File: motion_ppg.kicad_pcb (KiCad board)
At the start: 2 copper layers, 32.2 x 20.5 mm, 67 parts, among them P1 CONN_2, P2 CONN_2, P3 CONN_2, P4 CONN_1, P5 CONN_01X04, Q1 DMP21D5UFB4-7B, U1 TPS63001, U2 ADS1291/2, U3 NRF528XX-QFAA, U4 MPU-9250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

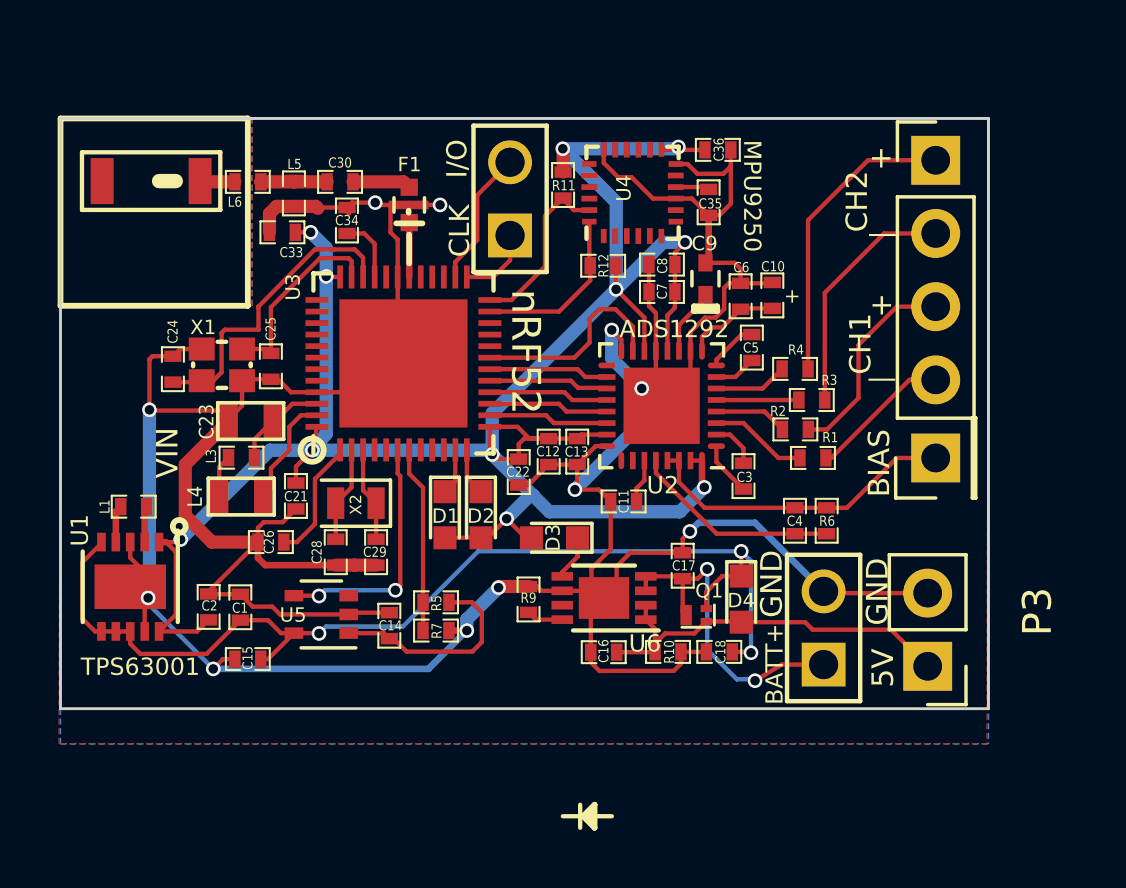
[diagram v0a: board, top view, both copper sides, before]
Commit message: Added new libs, removed load switch, added TPS62746
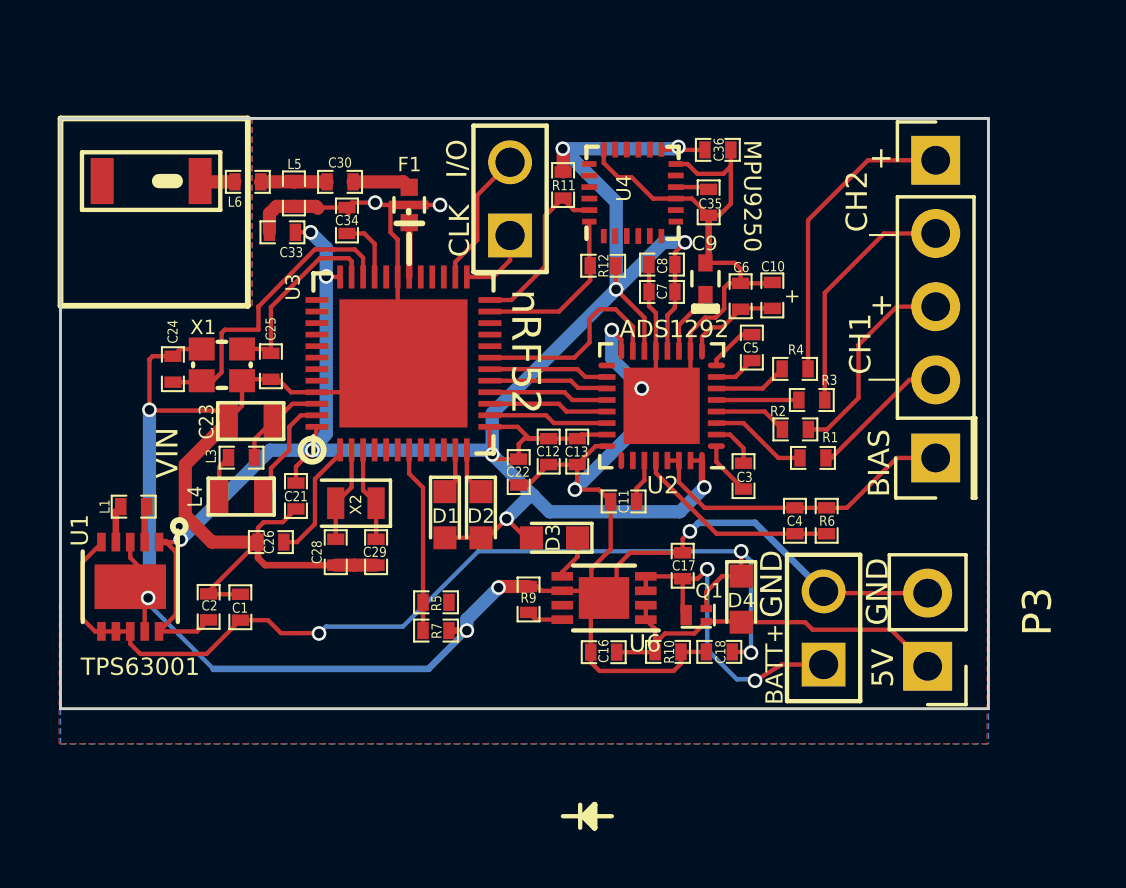
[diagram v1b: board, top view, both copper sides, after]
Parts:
- removed C14, C15: 10uF, SM0402
- removed U5: TPS2294x, TO_SOT_Packages_SMD:SOT-353_SC-70-5
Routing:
- net /LOAD_SW_CTRL: track 8.58 -> 0.00 mm, vias 2 -> 0
- net Net-(C14-Pad1): track 7.34 -> 0.00 mm
- net DGND: track 163.8 -> 157.5 mm, vias 11 -> 10
- net VCC: track 37.3 -> 35.7 mm

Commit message: Removed all components associated with ADS1292.
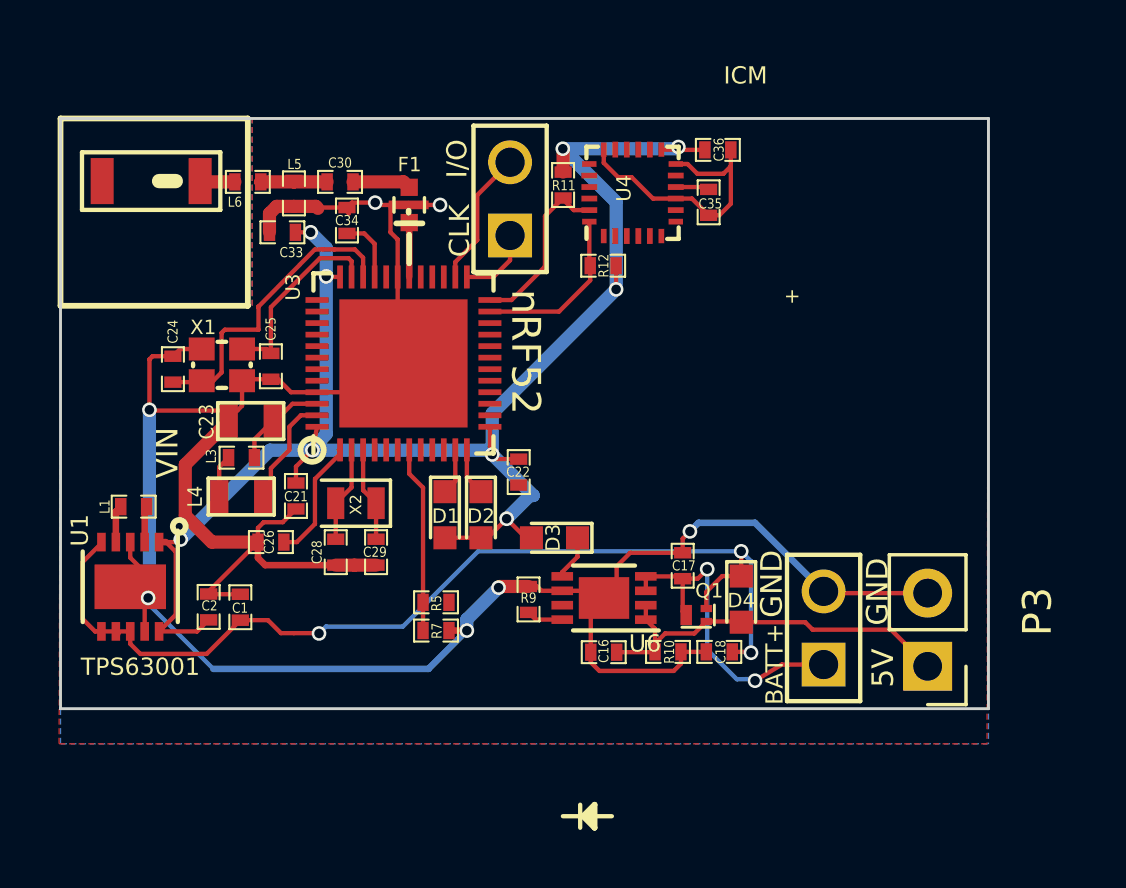
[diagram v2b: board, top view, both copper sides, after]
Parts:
- removed C10: 10uF, SM0402
- removed C11, C13, C8: 1uF, SM0402
- removed C12, C6, C7: 0.1uF, SM0402
- removed C3, C5: 4.7 nF, SM0402
- removed C4: 1.0nF-1.5nF, SM0402
- removed C9: 1uF, Capacitors_SMD:C_0402
- removed P4: CONN_1, Pin_Headers:Pin_Header_Straight_1x01_Pitch2.54mm
- removed P5: CONN_01X04, Pin_Headers:Pin_Header_Straight_1x04_Pitch2.54mm
- removed R1, R2, R3, R4: 30k, SM0402
- removed R6: 1MΩ, SM0402
- removed U2: ADS1291/2, Housings_DFN_QFN:QFN-32-1EP_4x4mm_Pitch0.4mm
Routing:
- net DGND: track 157.5 -> 121.2 mm, vias 10 -> 7
- net DVDD: track 82.4 -> 59.0 mm, vias 11 -> 9
- net /BIASIN: track 11.1 -> 0.00 mm
- net /IN2: track 10.5 -> 0.00 mm
- net /IN2-: track 8.42 -> 0.00 mm
- net /IN1: track 7.26 -> 0.00 mm
- net /~PWDN/RESET: track 7.23 -> 0.00 mm
- net Net-(C4-Pad1): track 7.23 -> 0.00 mm
- net /IN1-: track 4.93 -> 0.00 mm
- net /SPI_~CS: track 4.17 -> 0.00 mm
- net /SPI_SCLK: track 4.17 -> 0.00 mm
- net /DIN: track 4.17 -> 0.00 mm
- net /~DRDY: track 4.17 -> 0.00 mm
- net /DOUT: track 4.17 -> 0.00 mm
- net Net-(R1-Pad1): track 3.40 -> 0.00 mm
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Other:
- board text added: "ICM"
- board text removed: "ADS1292"
- board text removed: "BIAS"
- board text removed: "CH1"
- board text removed: "CH2"
- board text removed: "MPU9250"
- board text removed: "—"

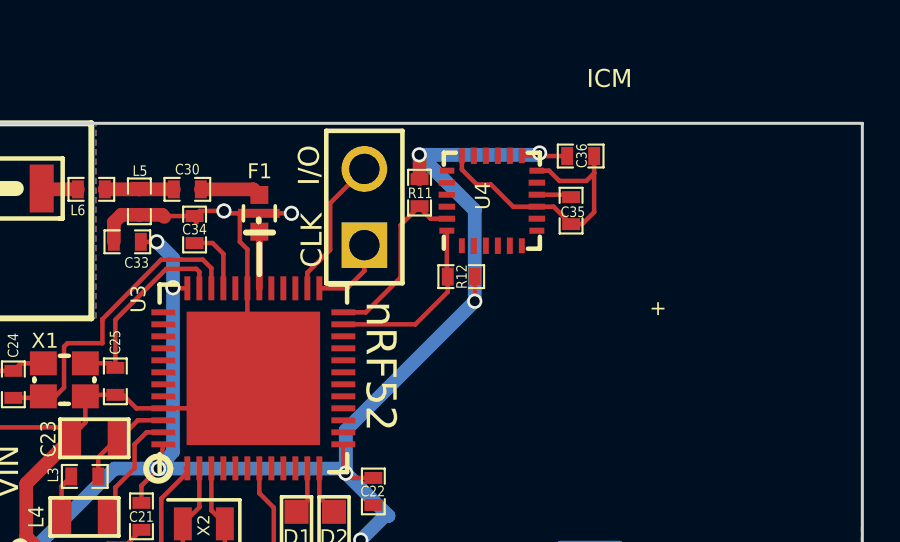
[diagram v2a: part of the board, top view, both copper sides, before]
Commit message: Fully updated ICM in PCB.
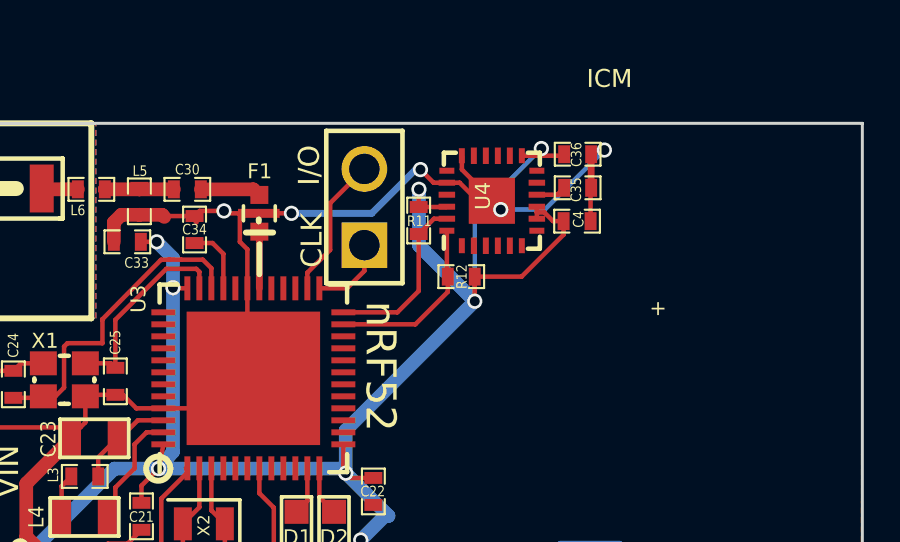
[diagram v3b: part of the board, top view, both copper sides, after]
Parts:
- added C4: 100nF, SM0402, F.Cu at (288.6, 128.8)
- U4: value MPU-9250 -> ICM-20948
- moved R11 0.93 mm to (283.3, 128.7)
- moved C35 0.79 mm to (288.6, 127.7), turned to 180 degrees
- moved C36 0.12 mm to (288.6, 126.5), turned to 180 degrees
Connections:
- C35 pad 1: Net-(C35-Pad1) -> DGND
- C35 pad 2: DGND -> Net-(C35-Pad2)
- C36 pad 1: DVDD -> DGND
- C36 pad 2: DGND -> DVDD
- R5 pad 1: /AIN_BAT_DIV_VOLTAGE -> Net-(R5-Pad1)
- R5 pad 2: Net-(C14-Pad1) -> /AIN_BAT_DIV_VOLTAGE
- U4 pad 10: Net-(C35-Pad1) -> Net-(C35-Pad2)
- U4 pad 12: DGND -> Net-(U4-Pad12)
- U4 pad 20: Net-(U4-Pad20) -> DGND
- U4 pad 22: Net-(U4-Pad22) -> DVDD
- U4 pad 8: Net-(U4-Pad8) -> DVDD
- U4 pad 9: DGND -> DVDD
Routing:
- net DVDD: track 59.0 -> 66.0 mm
- net DGND: track 121.2 -> 128.1 mm, vias 7 -> 10
- net Net-(C35-Pad1): track 1.17 -> 0.00 mm
- net Net-(C35-Pad2): track 0.00 -> 1.01 mm

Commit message: Fixed netlist for ICM (3V3→1V8)
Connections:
- C36 pad 2: DVDD -> 1.8V
- C4 pad 1: DVDD -> 1.8V
- R11 pad 1: DVDD -> 1.8V
- R12 pad 1: DVDD -> 1.8V
- U4 pad 13: DVDD -> 1.8V
- U4 pad 22: DVDD -> 1.8V
- U4 pad 8: DVDD -> 1.8V
- U4 pad 9: DVDD -> 1.8V
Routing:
- net DVDD: track 66.0 -> 40.0 mm, vias 9 -> 6
- net 1.8V: track 0.00 -> 19.9 mm, vias 0 -> 3
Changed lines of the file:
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@@
     (thickness 1.6)
     (drawings 35)
-    (tracks 381)
+    (tracks 380)
     (zones 0)
     (modules 46)
-    (nets 76)
+    (nets 77)
   )
   (page A3)
@@
   )
   (setup
-    (last_trace_width 0.152)
+    (last_trace_width 0.4572)
     (user_trace_width 0.152)
     (user_trace_width 0.229)
@@
   (net 74 "Net-(R5-Pad1)")
   (net 75 "Net-(U4-Pad12)")
+  (net 76 1.8V)
   (net_class Default "This is the default net class."
     (clearance 0.1524)
@@
     (add_net /~DRDY)
     (add_net /~PWDN/RESET)
+    (add_net 1.8V)
     (add_net 5V_in_charge)
     (add_net DGND)
@@
       (net 62 DGND))
     (pad 1 smd rect (at -0.44958 0) (size 0.39878 0.59944) (layers F.Cu F.Paste F.Mask)
-      (net 12 DVDD))
+      (net 76 1.8V))
     (model smd\chip_cms.wrl
       (offset (xyz 0 0 0.05079999923706055))
@@
       (net 54 "Net-(U4-Pad7)"))
     (pad 8 smd rect (at -0.6 1.5 180) (size 0.55 0.2) (layers F.Cu F.Paste F.Mask)
-      (net 12 DVDD))
+      (net 76 1.8V))
     (pad 9 smd rect (at -0.2 1.5 180) (size 0.55 0.2) (layers F.Cu F.Paste F.Mask)
-      (net 12 DVDD))
+      (net 76 1.8V))
     (pad 10 smd rect (at 0.2 1.5 180) (size 0.55 0.2) (layers F.Cu F.Paste F.Mask)
       (net 73 "Net-(C35-Pad2)"))
@@
       (net 75 "Net-(U4-Pad12)"))
     (pad 13 smd rect (at 1.5 1 90) (size 0.5 0.2) (layers F.Cu F.Paste F.Mask)
-      (net 12 DVDD))
+      (net 76 1.8V))
     (pad 14 smd rect (at 1.5 0.6 90) (size 0.55 0.2) (layers F.Cu F.Paste F.Mask)
       (net 56 "Net-(U4-Pad14)"))
@@
       (net 61 "Net-(U4-Pad21)"))
     (pad 22 smd rect (at -0.2 -1.5 180) (size 0.55 0.2) (layers F.Cu F.Paste F.Mask)
-      (net 12 DVDD))
+      (net 76 1.8V))
     (pad 23 smd rect (at -0.6 -1.5 180) (size 0.55 0.2) (layers F.Cu F.Paste F.Mask)
       (net 47 /SCL))
@@
     (fp_line (start 0.762 0.381) (end 0.254 0.381) (layer F.SilkS) (width 0.07112))
     (pad 1 smd rect (at -0.44958 0 180) (size 0.39878 0.59944) (layers F.Cu F.Paste F.Mask)
-      (net 12 DVDD))
+      (net 76 1.8V))
     (pad 2 smd rect (at 0.44958 0 180) (size 0.39878 0.59944) (layers F.Cu F.Paste F.Mask)
       (net 46 /SDI))
@@
     (fp_line (start 0.762 0.381) (end 0.254 0.381) (layer F.SilkS) (width 0.07112))
     (pad 1 smd rect (at -0.44958 0 270) (size 0.39878 0.59944) (layers F.Cu F.Paste F.Mask)
-      (net 12 DVDD))
+      (net 76 1.8V))
     (pad 2 smd rect (at 0.44958 0 270) (size 0.39878 0.59944) (layers F.Cu F.Paste F.Mask)
       (net 47 /SCL))
@@
       (net 62 DGND))
     (pad 2 smd rect (at 0.44958 0 180) (size 0.39878 0.59944) (layers F.Cu F.Paste F.Mask)
-      (net 12 DVDD))
+      (net 76 1.8V))
     (model smd\chip_cms.wrl
       (offset (xyz 0 0 0.05079999923706055))
@@
   (segment (start 281.04042 137.32042) (end 280.88 137.16) (width 0.152) (layer F.Cu) (net 12))
   (segment (start 280.88 137.16) (end 280.88 135.72916) (width 0.4572) (layer B.Cu) (net 12))
-  (segment (start 280.88 135.72916) (end 285.17958 131.42958) (width 0.4572) (layer B.Cu) (net 12))
-  (segment (start 285.17958 131.37) (end 285.17958 131.42958) (width 0.152) (layer F.Cu) (net 12))
-  (segment (start 285.17958 130.61) (end 285.17958 131.37) (width 0.152) (layer F.Cu) (net 12))
-  (via (at 285.17958 131.42958) (size 0.508) (drill 0.3302) (layers F.Cu B.Cu) (net 12))
+  (segment (start 285.17958 131.37) (end 285.17958 131.42958) (width 0.152) (layer F.Cu) (net 76))
+  (segment (start 285.17958 130.61) (end 285.17958 131.37) (width 0.152) (layer F.Cu) (net 76))
+  (via (at 285.17958 131.42958) (size 0.508) (drill 0.3302) (layers F.Cu B.Cu) (net 76))
   (segment (start 269.32 140.2) (end 269.98 140.2) (width 0.152) (layer F.Cu) (net 12))
   (segment (start 273.17 137.01) (end 274.64 137.01) (width 0.4572) (layer B.Cu) (net 12))
@@
   (via (at 274.58 129.45) (size 0.508) (drill 0.3302) (layers F.Cu B.Cu) (net 12))
   (segment (start 280.8 136.2) (end 280.8 136.89) (width 0.152) (layer F.Cu) (net 12))
-  (segment (start 284.24 128.29) (end 284.25 128.28) (width 0.152) (layer F.Cu) (net 12))
-  (segment (start 283.31 128.29) (end 284.24 128.29) (width 0.152) (layer F.Cu) (net 12))
-  (via (at 283.32 127.7) (size 0.508) (drill 0.3302) (layers F.Cu B.Cu) (net 12))
-  (segment (start 283.31 128.29) (end 283.31 127.71) (width 0.152) (layer F.Cu) (net 12))
-  (segment (start 283.31 127.71) (end 283.32 127.7) (width 0.152) (layer F.Cu) (net 12))
-  (segment (start 283.32 129.57) (end 283.32 127.7) (width 0.4572) (layer B.Cu) (net 12))
-  (segment (start 285.17958 131.42958) (end 283.32 129.57) (width 0.4572) (layer B.Cu) (net 12))
-  (segment (start 288.11084 126.58) (end 288.16084 126.53) (width 0.152) (layer F.Cu) (net 12))
-  (via (at 287.4 126.34) (size 0.508) (drill 0.3302) (layers F.Cu B.Cu) (net 12))
-  (segment (start 285.17958 131.42958) (end 285.17958 128.56042) (width 0.152) (layer B.Cu) (net 12))
-  (segment (start 285.17958 128.56042) (end 287.4 126.34) (width 0.152) (layer B.Cu) (net 12))
-  (segment (start 287.41 126.35) (end 287.41 126.58) (width 0.152) (layer F.Cu) (net 12))
-  (segment (start 287.4 126.34) (end 287.41 126.35) (width 0.152) (layer F.Cu) (net 12))
-  (segment (start 286.75 126.58) (end 287.41 126.58) (width 0.152) (layer F.Cu) (net 12))
-  (segment (start 287.41 126.58) (end 288.11084 126.58) (width 0.152) (layer F.Cu) (net 12))
-  (segment (start 287.78945 128.76) (end 288.14084 128.76) (width 0.152) (layer F.Cu) (net 12))
-  (segment (start 287.49945 128.47) (end 287.78945 128.76) (width 0.152) (layer F.Cu) (net 12))
-  (segment (start 287.25 128.47) (end 287.49945 128.47) (width 0.152) (layer F.Cu) (net 12))
-  (segment (start 287.25 128.47) (end 287.25 128.68) (width 0.152) (layer F.Cu) (net 12))
-  (segment (start 287.25 128.28) (end 287.25 128.47) (width 0.152) (layer F.Cu) (net 12))
-  (segment (start 288.14084 129.21172) (end 288.14084 128.76) (width 0.152) (layer F.Cu) (net 12))
-  (segment (start 286.74256 130.61) (end 288.14084 129.21172) (width 0.152) (layer F.Cu) (net 12))
-  (segment (start 285.17958 130.61) (end 286.74256 130.61) (width 0.152) (layer F.Cu) (net 12))
+  (segment (start 284.24 128.29) (end 284.25 128.28) (width 0.152) (layer F.Cu) (net 76))
+  (segment (start 283.31 128.29) (end 284.24 128.29) (width 0.152) (layer F.Cu) (net 76))
+  (via (at 283.32 127.7) (size 0.508) (drill 0.3302) (layers F.Cu B.Cu) (net 76))
+  (segment (start 283.31 128.29) (end 283.31 127.71) (width 0.152) (layer F.Cu) (net 76))
+  (segment (start 283.31 127.71) (end 283.32 127.7) (width 0.152) (layer F.Cu) (net 76))
+  (segment (start 283.32 129.57) (end 283.32 127.7) (width 0.4572) (layer B.Cu) (net 76))
+  (segment (start 285.17958 131.42958) (end 283.32 129.57) (width 0.4572) (layer B.Cu) (net 76))
+  (segment (start 288.11084 126.58) (end 288.16084 126.53) (width 0.152) (layer F.Cu) (net 76))
+  (via (at 287.4 126.34) (size 0.508) (drill 0.3302) (layers F.Cu B.Cu) (net 76))
+  (segment (start 285.17958 131.42958) (end 285.17958 128.56042) (width 0.152) (layer B.Cu) (net 76))
+  (segment (start 285.17958 128.56042) (end 287.4 126.34) (width 0.152) (layer B.Cu) (net 76))
+  (segment (start 287.41 126.35) (end 287.41 126.58) (width 0.152) (layer F.Cu) (net 76))
+  (segment (start 287.4 126.34) (end 287.41 126.35) (width 0.152) (layer F.Cu) (net 76))
+  (segment (start 286.75 126.58) (end 287.41 126.58) (width 0.152) (layer F.Cu) (net 76))
+  (segment (start 287.41 126.58) (end 288.11084 126.58) (width 0.152) (layer F.Cu) (net 76))
+  (segment (start 287.78945 128.76) (end 288.14084 128.76) (width 0.152) (layer F.Cu) (net 76))
+  (segment (start 287.49945 128.47) (end 287.78945 128.76) (width 0.152) (layer F.Cu) (net 76))
+  (segment (start 287.25 128.47) (end 287.49945 128.47) (width 0.152) (layer F.Cu) (net 76))
+  (segment (start 287.25 128.47) (end 287.25 128.68) (width 0.152) (layer F.Cu) (net 76))
+  (segment (start 287.25 128.28) (end 287.25 128.47) (width 0.152) (layer F.Cu) (net 76))
+  (segment (start 288.14084 129.21172) (end 288.14084 128.76) (width 0.152) (layer F.Cu) (net 76))
+  (segment (start 286.74256 130.61) (end 288.14084 129.21172) (width 0.152) (layer F.Cu) (net 76))
+  (segment (start 285.17958 130.61) (end 286.74256 130.61) (width 0.152) (layer F.Cu) (net 76))
   (segment (start 289.52 141.38) (end 289.52 140.52) (width 0.152) (layer F.Cu) (net 15))
   (via (at 289.52 140.52) (size 0.508) (drill 0.3302) (layers F.Cu B.Cu) (net 15))

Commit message: Fully realized schematic and pcb awaiting final check.
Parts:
- added C10: 2.2 uF, SM0402, F.Cu at (290.2, 135.8)
- added C3: 10uF, SM0402, F.Cu at (276.6, 143.5)
- added C5: 10uF, SM0402, F.Cu at (277.4, 142.8)
- added C6: 2.2uF, SM0402, F.Cu at (284.9, 134.8)
- added C7: 4.7uF, SM0402, F.Cu at (287.0, 132.7)
- added C9: 4.7uF, SM0402, F.Cu at (288.6, 133.8)
- added IC1: SFH_7070, SFH_7070:SFH7070, B.Cu at (280.4, 134.3)
- added L2: 2.20µH, Inductor_SMD:L_0603_1608Metric, F.Cu at (273.8, 143.6)
- added R1: 470, SM0402, F.Cu at (286.5, 131.7)
- added R2: 12k, SM0402, F.Cu at (286.5, 133.7)
- added R3: 100k, SM0402, F.Cu at (287.7, 136.6)
- added R4: 100k, SM0402, F.Cu at (287.7, 138.4)
- added R6: 10k, SM0402, F.Cu at (287.7, 135.2)
- added R8: 3.3M, SM0402, F.Cu at (285.3, 138.9)
- added U2: TPS62746, Package_BGA:Texas_DSBGA-8_0.9x1.9mm_Layout2x4_P0.5mm, F.Cu at (275.4, 143.4)
- added U5: MCP6001-OT, Package_TO_SOT_SMD:SOT-353_SC-70-5, F.Cu at (285.1, 136.9)
- L1: footprint SM0402 -> Inductor_SMD:L_0603_1608Metric
- moved R5 1.03 mm to (278.9, 143.3)
- moved R7 0.91 mm to (278.9, 142.4), turned to 0 degrees
- moved L1 0.20 mm to (268.2, 138.9)
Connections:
- U3 pad 5: Net-(U3-Pad5) -> /LOAD_SW_CTRL
- U3 pad 6: /LOAD_SW_CTRL -> /AIN_BAT_DIV_VOLTAGE
- U3 pad 7: /AIN_BAT_DIV_VOLTAGE -> /ppg_amp_out
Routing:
- net 1.8V: track 19.9 -> 45.7 mm, vias 3 -> 5
- net DVDD: track 40.0 -> 53.7 mm, vias 6 -> 5
- net VCC: track 35.7 -> 49.2 mm, vias 3 -> 4
- net /LOAD_SW_CTRL: track 0.00 -> 11.1 mm, vias 0 -> 2
- net Net-(IC1-Pad1): track 0.00 -> 10.7 mm, vias 0 -> 1
- net /ppg_amp_out: track 0.00 -> 8.36 mm, vias 0 -> 2
- net Net-(C7-Pad2): track 0.00 -> 7.97 mm, vias 0 -> 1
- net Net-(C10-Pad1): track 0.00 -> 6.02 mm
- net Net-(R6-Pad2): track 0.00 -> 5.75 mm, vias 0 -> 2
- net DGND: track 128.1 -> 133.4 mm, vias 10 -> 11
- net Net-(R5-Pad1): track 0.00 -> 3.97 mm
- net Net-(C10-Pad2): track 0.00 -> 3.41 mm
- net Net-(C7-Pad1): track 0.00 -> 1.56 mm
- net Net-(L2-Pad1): track 0.00 -> 1.48 mm
- net /AIN_BAT_DIV_VOLTAGE: track 6.47 -> 7.03 mm
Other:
- board text added: "Motion-PPG Prototype Yeo GaTech BNE Lab 04/04/2019"
- board text removed: "+"
- board text removed: "nRF52-ADS1292-MPU ExG Prototype - 06/08/18 Yeo GaTech BNE Lab"
